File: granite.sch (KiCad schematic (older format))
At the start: 33 parts, among them CON1 USB-MINI-B WM17115-ND, IC1 ATMEGA32U4, SW1 SW423CT-ND, Y1 16MHz

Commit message: updated schematic for full 60% keyboard TODO: matrix pin assignments are temp TODO: add NPNs for RGB LEDs TODO: may want to consider a second set of LED outputs for a second PWM phase?
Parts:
- added D0:3, D0:4, D0:5, D0:6, D0:7, D0:8, D0:9, D0:A, D0:B, D0:C, D0:D, D1:3, D1:4, D1:5, D1:6, D1:7, D1:8, D1:9, D1:A, D1:B, D1:C, D1:D, D2:2, D2:3, D2:4, D2:5, D2:6, D2:7, D2:8, D2:9, D2:A, D2:B, D2:C, D2:D, D3:0, D3:1, D3:2, D3:3, D3:4, D3:5, D3:6, D3:7, D3:8, D3:9, D3:A, D3:B, D3:C, D3:D, D4:0, D4:1, D4:2, D4:3, D4:5, D4:6, D4:8, D4:A, D4:B, D4:C, D4:D, S2:0: D, SM0805:SOD-123, symbol D
- added S0:3: K_3, bwu-keyboard:bwu-mx1a-1u, symbol MX1A
- added S0:4: K_4, bwu-keyboard:bwu-mx1a-1u, symbol MX1A
- added S0:5: K_5, bwu-keyboard:bwu-mx1a-1u, symbol MX1A
- added S0:6: K_BL1, bwu-keyboard:bwu-mx1a-1u, symbol MX1A
- added S0:7: K_BL2, bwu-keyboard:bwu-mx1a-1u, symbol MX1A
- added S0:8: K_6, bwu-keyboard:bwu-mx1a-1u, symbol MX1A
- added S0:9: K_7, bwu-keyboard:bwu-mx1a-1u, symbol MX1A
- added S0:A: K_8, bwu-keyboard:bwu-mx1a-1u, symbol MX1A
- added S0:B: K_9, bwu-keyboard:bwu-mx1a-1u, symbol MX1A
- added S0:C: K_0, bwu-keyboard:bwu-mx1a-1u, symbol MX1A
- added S0:D: K_EQUAL, bwu-keyboard:bwu-mx1a-1u, symbol MX1A
- added S1:3: K_PRD, bwu-keyboard:bwu-mx1a-1u, symbol MX1A
- added S1:4: K_P, bwu-keyboard:bwu-mx1a-1u, symbol MX1A
- added S1:5: K_Y, bwu-keyboard:bwu-mx1a-1u, symbol MX1A
- added S1:6: K_HOME, bwu-keyboard:bwu-mx1a-1u, symbol MX1A
- added S1:7: K_PGUP, bwu-keyboard:bwu-mx1a-1u, symbol MX1A
- added S1:8: K_F, bwu-keyboard:bwu-mx1a-1u, symbol MX1A
- added S1:9: K_G, bwu-keyboard:bwu-mx1a-1u, symbol MX1A
- added S1:A: K_C, bwu-keyboard:bwu-mx1a-1u, symbol MX1A
- added S1:B: K_R, bwu-keyboard:bwu-mx1a-1u, symbol MX1A
- added S1:C: K_L, bwu-keyboard:bwu-mx1a-1u, symbol MX1A
- added S1:D: K_SLASH, bwu-keyboard:bwu-mx1a-1u, symbol MX1A
- added S2:0: K_BKTK, bwu-keyboard:bwu-mx1a-1u, symbol MX1A
- added S2:2: K_O, bwu-keyboard:bwu-mx1a-1u, symbol MX1A
- added S2:3: K_E, bwu-keyboard:bwu-mx1a-1u, symbol MX1A
- added S2:4: K_U, bwu-keyboard:bwu-mx1a-1u, symbol MX1A
- added S2:5: K_I, bwu-keyboard:bwu-mx1a-1u, symbol MX1A
- added S2:6: K_END, bwu-keyboard:bwu-mx1a-1u, symbol MX1A
- added S2:7: K_PGDN, bwu-keyboard:bwu-mx1a-1u, symbol MX1A
- added S2:8: K_D, bwu-keyboard:bwu-mx1a-1u, symbol MX1A
- added S2:9: K_H, bwu-keyboard:bwu-mx1a-1u, symbol MX1A
- added S2:A: K_T, bwu-keyboard:bwu-mx1a-1u, symbol MX1A
- added S2:B: K_N, bwu-keyboard:bwu-mx1a-1u, symbol MX1A
- added S2:C: K_S, bwu-keyboard:bwu-mx1a-1u, symbol MX1A
- added S2:D: K_DASH, bwu-keyboard:bwu-mx1a-1u, symbol MX1A
- added S3:0: K_LSHFT, bwu-keyboard:bwu-mx1a-1u, symbol MX1A
- added S3:1: K_SMCLN, bwu-keyboard:bwu-mx1a-1u, symbol MX1A
- added S3:2: K_Q, bwu-keyboard:bwu-mx1a-1u, symbol MX1A
- added S3:3: K_J, bwu-keyboard:bwu-mx1a-1u, symbol MX1A
- added S3:4: K_K, bwu-keyboard:bwu-mx1a-1u, symbol MX1A
- added S3:5: K_X, bwu-keyboard:bwu-mx1a-1u, symbol MX1A
- added S3:6: K_DEL, bwu-keyboard:bwu-mx1a-1u, symbol MX1A
- added S3:7: K_INS, bwu-keyboard:bwu-mx1a-1u, symbol MX1A
- added S3:8: K_B, bwu-keyboard:bwu-mx1a-1u, symbol MX1A
- added S3:9: K_M, bwu-keyboard:bwu-mx1a-1u, symbol MX1A
- added S3:A: K_W, bwu-keyboard:bwu-mx1a-1u, symbol MX1A
- added S3:B: K_V, bwu-keyboard:bwu-mx1a-1u, symbol MX1A
- added S3:C: K_Z, bwu-keyboard:bwu-mx1a-1u, symbol MX1A
- added S3:D: K_RSHFT, bwu-keyboard:bwu-mx1a-1u, symbol MX1A
- added S4:0: K_LCTRL, bwu-keyboard:bwu-mx1a-1u, symbol MX1A
- added S4:1: K_LGUI, bwu-keyboard:bwu-mx1a-1u, symbol MX1A
- added S4:2: K_LALT, bwu-keyboard:bwu-mx1a-1u, symbol MX1A
- added S4:3: K_LFN, bwu-keyboard:bwu-mx1a-1u, symbol MX1A
- added S4:5: K_BKSPC, bwu-keyboard:bwu-mx1a-1u, symbol MX1A
- added S4:6: K_SPACE, bwu-keyboard:bwu-mx1a-1u, symbol MX1A
- added S4:8: K_ENTER, bwu-keyboard:bwu-mx1a-1u, symbol MX1A
- added S4:A: K_RFN, bwu-keyboard:bwu-mx1a-1u, symbol MX1A
- added S4:B: K_RALT, bwu-keyboard:bwu-mx1a-1u, symbol MX1A
- added S4:C: K_RGUI, bwu-keyboard:bwu-mx1a-1u, symbol MX1A
- added S4:D: K_RCTRL, bwu-keyboard:bwu-mx1a-1u, symbol MX1A
- S0:0: value MX1A -> K_ESC
- S0:1: value MX1A -> K_1
- S0:2: value MX1A -> K_2
- S1:0: value MX1A -> K_TAB
- S1:1: value MX1A -> K_QUOTE
- S1:2: value MX1A -> K_COMMA
- S2:1: value MX1A -> K_A; footprint bwu-keyboard:bwu-mx1a-2u -> bwu-keyboard:bwu-mx1a-1u
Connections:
- net labels added: C3, C4, C5, C6, C7, C8, C9, CA, CB, CC, CD, R3, R4
- wire segments 59 -> 192
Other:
- moved on the sheet: C1, C2, C3, C4, C5, C6, C7, C8, CON1, D0:0, D0:1, D0:2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

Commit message: first routing pass finished
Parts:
- added LED2, LED3, LED4, LED5, LED6, LED7: 5060BRG4, bwu-keyboard:bwu-5060BRG4, symbol 5060BRG4
- added Q1, Q2, Q3: NMOSFET, bwu-keyboard:IRLML2502, symbol NMOSFET
- added R10, R12, R13, R15, R16, R18, R19, R21, R22, R24, R7, R9: 220Ω, bwu-keyboard:bwu-resistor-0805, symbol R
- added R11, R14, R17, R20, R23, R8: 330Ω, bwu-keyboard:bwu-resistor-0805, symbol R
- added R25, R26, R27: 1kΩ, bwu-keyboard:bwu-resistor-0805, symbol R
- S0:0, S1:0, S2:0, S3:0, S4:5, S4:8: footprint bwu-keyboard:bwu-mx1a-1u -> bwu-keyboard:bwu-mx1a-150u
- S0:13: renamed from S0:D; footprint bwu-keyboard:bwu-mx1a-1u -> bwu-keyboard:bwu-mx1a-150u
- S1:13: renamed from S1:D; footprint bwu-keyboard:bwu-mx1a-1u -> bwu-keyboard:bwu-mx1a-150u
- S2:13: renamed from S2:D; footprint bwu-keyboard:bwu-mx1a-1u -> bwu-keyboard:bwu-mx1a-150u
- S3:13: renamed from S3:D; footprint bwu-keyboard:bwu-mx1a-1u -> bwu-keyboard:bwu-mx1a-150u
- S4:0, S4:1, S4:2, S4:3: footprint bwu-keyboard:bwu-mx1a-1u -> bwu-keyboard:bwu-mx1a-125u
- S4:10: renamed from S4:A; footprint bwu-keyboard:bwu-mx1a-1u -> bwu-keyboard:bwu-mx1a-125u
- S4:11: renamed from S4:B; footprint bwu-keyboard:bwu-mx1a-1u -> bwu-keyboard:bwu-mx1a-125u
- S4:12: renamed from S4:C; footprint bwu-keyboard:bwu-mx1a-1u -> bwu-keyboard:bwu-mx1a-125u
- S4:13: renamed from S4:D; footprint bwu-keyboard:bwu-mx1a-1u -> bwu-keyboard:bwu-mx1a-125u
- S4:6: footprint bwu-keyboard:bwu-mx1a-1u -> bwu-keyboard:bwu-mx1a-2u
- renumbered D0:A to D0:10, D0:B to D0:11, D0:C to D0:12, D0:D to D0:13, D1:A to D1:10, D1:B to D1:11, D1:C to D1:12, D1:D to D1:13, S2:0 to D2:0, D2:A to D2:10, D2:B to D2:11, D2:C to D2:12, D2:D to D2:13, D3:A to D3:10, D3:B to D3:11, D3:C to D3:12, D3:D to D3:13, D4:A to D4:10, D4:B to D4:11, D4:C to D4:12, D4:D to D4:13, S0:A to S0:10, S0:B to S0:11, S0:C to S0:12, S1:A to S1:10, S1:B to S1:11, S1:C to S1:12, S2:A to S2:10, S2:B to S2:11, S2:C to S2:12, S3:A to S3:10, S3:B to S3:11, S3:C to S3:12
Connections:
- net labels added: LED_B_CTL, LED_B_Q, LED_G_CTL, LED_G_Q, LED_R_CTL, LED_R_Q, USB_D+, USB_D-
- net labels removed: LED_B, LED_G, LED_R
- wire segments 192 -> 240
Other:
- moved on the sheet: R1, R2, R4, R5, R6

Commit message: replacing mosfets with dedicated led driver chip
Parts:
- removed Q1, Q2, Q3: NMOSFET, bwu-keyboard:IRLML2502, symbol NMOSFET
- removed R10, R12, R13, R15, R16, R18, R19, R21, R22, R24, R9: 220Ω, bwu-keyboard:bwu-resistor-0805, symbol R
- removed R11, R14, R17, R20, R23: 330Ω, bwu-keyboard:bwu-resistor-0805, symbol R
- removed R25, R26, R27: 1kΩ, bwu-keyboard:bwu-resistor-0805, symbol R
- added C10: 100nF, symbol C
- added C9: 220nF, symbol C
- added IC2: IS31FL3731, symbol IS31FL3731
- R4, R6: value 220Ω -> 4.7kΩ
- R5: value 330Ω -> 4.7kΩ
- R7: value 220Ω -> 100kΩ
- R8: value 330Ω -> 20kΩ
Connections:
- net labels added: CA1, CA2, CA3, CA4, CA5, CA6, CA7, CA8, CA9, INTB, SCL, SDA, SDB
- net labels removed: LED_B_CTL, LED_B_Q, LED_G_CTL, LED_G_Q, LED_R_CTL, LED_R_Q
- wire segments 240 -> 212
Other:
- moved on the sheet: R4, R5, R6, R7, R8

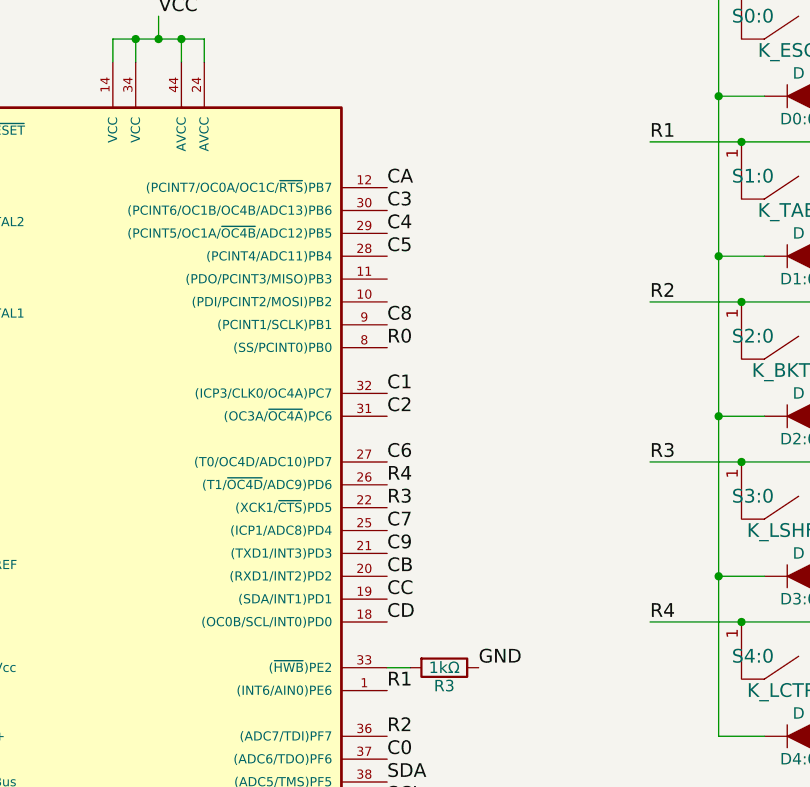
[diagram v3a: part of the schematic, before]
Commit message: some routing cleanup
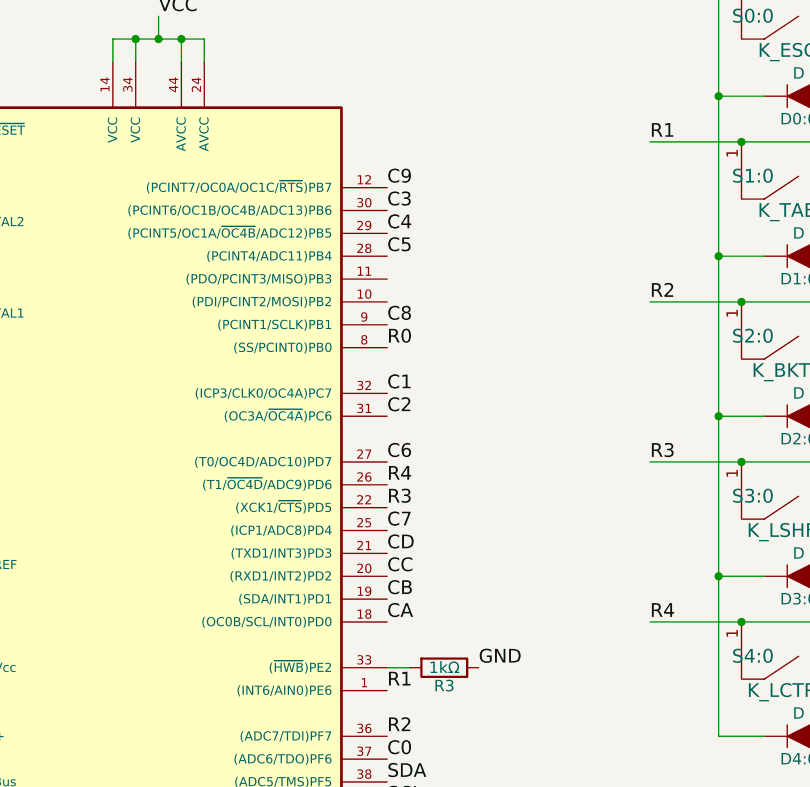
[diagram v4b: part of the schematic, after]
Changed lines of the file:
@@
 Text Label 3950 4300 0    60   ~ 0
 C8
+Text Label 3950 3700 0    60   ~ 0
+C9
+Text Label 3950 5600 0    60   ~ 0
+CA
+Text Label 3950 5500 0    60   ~ 0
+CB
+Text Label 3950 5400 0    60   ~ 0
+CC
 Text Label 3950 5300 0    60   ~ 0
-C9
-Text Label 3950 3700 0    60   ~ 0
-CA
-Text Label 3950 5400 0    60   ~ 0
-CB
-Text Label 3950 5500 0    60   ~ 0
-CC
-Text Label 3950 5600 0    60   ~ 0
 CD
 $Comp
